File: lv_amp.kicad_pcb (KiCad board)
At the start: 2 copper layers, 127 x 76.2 mm, 85 parts, among them J1 Jack-DC, J2 AudioJack2, J3 AudioJack2, Q1 Q_NMOS_DGS, U1 MAX1771xSA, U2 TL072, U3 ECC83, U4 ECC83, U5 ECC83

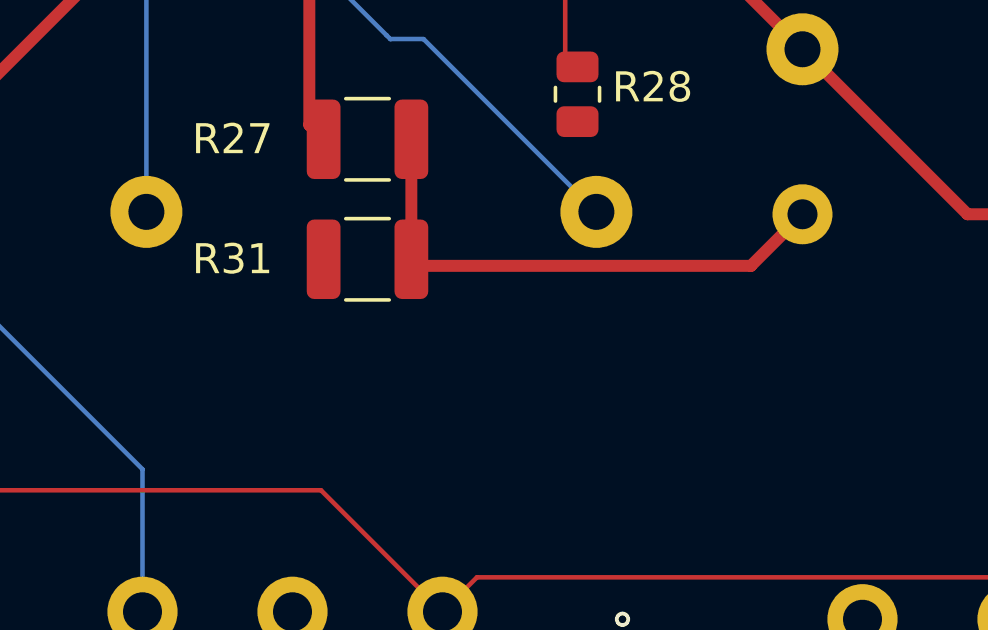
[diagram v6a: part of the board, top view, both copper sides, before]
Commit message: alpha0 errata: add 0ohm resistor for easier modding of stage 4
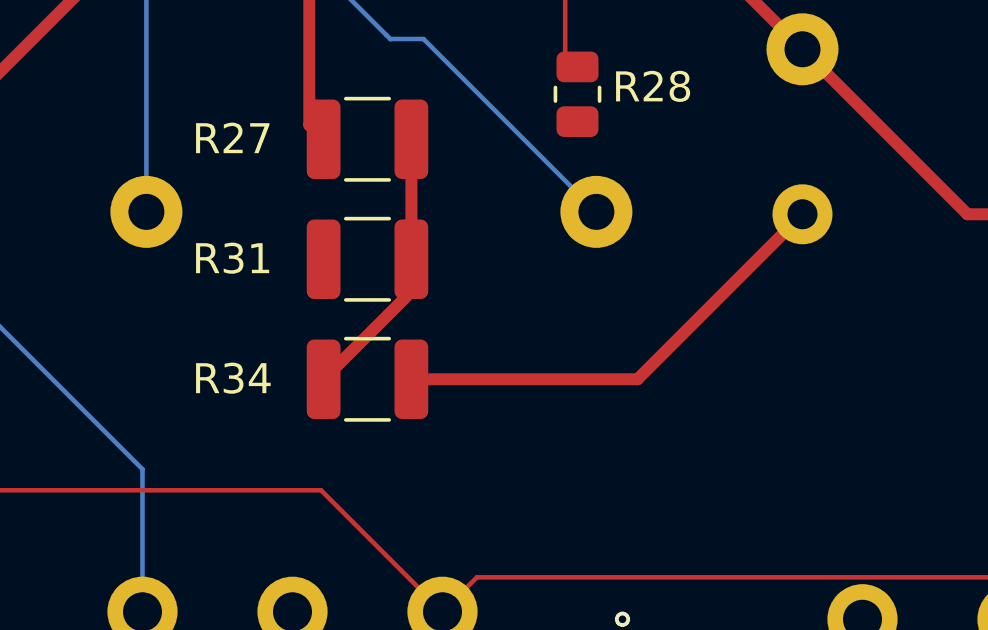
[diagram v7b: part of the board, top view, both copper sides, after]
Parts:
- added R34: 0, Resistor_SMD:R_1210_3225Metric, F.Cu at (81.5, 129.0)
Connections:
- C22 pad 2: /u3ap_couple -> /u3ap_couple_res
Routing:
- net /u3ap_couple_res: track 0.00 -> 15.3 mm
- net /u3ap_couple: track 17.8 -> 9.21 mm
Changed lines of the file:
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@@
   (net 54 "unconnected-(U5-Pad9)")
   (net 55 "/q1gr")
+  (net 56 "/u3ap_couple_res")
   (footprint "Capacitor_SMD:C_0603_1608Metric" (layer "F.Cu")
     (at 55 87 -90)
@@
   )
   (footprint "Resistor_SMD:R_1210_3225Metric" (layer "F.Cu")
+    (at 81.5 129)
+    (descr "Resistor SMD 1210 (3225 Metric), square (rectangular) end terminal, IPC_7351 nominal, (Body size source: IPC-SM-782 page 72, https://www.pcb-3d.com/wordpress/wp-content/uploads/ipc-sm-782a_amendment_1_and_2.pdf), generated with kicad-footprint-generator")
+    (tags "resistor")
+    (property "Sheetfile" "lv_amp.kicad_sch")
+    (property "Sheetname" "")
+    (attr smd)
+    (fp_text reference "R34" (at -4.5 0) (layer "F.SilkS")
+      (effects (font (size 1 1) (thickness 0.15)))
+    )
+    (fp_text value "0" (at 0 2.28) (layer "F.Fab")
+      (effects (font (size 1 1) (thickness 0.15)))
+    )
+    (fp_text user "${REFERENCE}" (at 0 0) (layer "F.Fab")
+      (effects (font (size 0.8 0.8) (thickness 0.12)))
+    )
+    (fp_line (start -0.723737 1.355) (end 0.723737 1.355) (layer "F.SilkS") (width 0.12))
+    (fp_line (start -0.723737 -1.355) (end 0.723737 -1.355) (layer "F.SilkS") (width 0.12))
+    (fp_line (start 2.28 1.58) (end -2.28 1.58) (layer "F.CrtYd") (width 0.05))
+    (fp_line (start 2.28 -1.58) (end 2.28 1.58) (layer "F.CrtYd") (width 0.05))
+    (fp_line (start -2.28 -1.58) (end 2.28 -1.58) (layer "F.CrtYd") (width 0.05))
+    (fp_line (start -2.28 1.58) (end -2.28 -1.58) (layer "F.CrtYd") (width 0.05))
+    (fp_line (start -1.6 1.245) (end -1.6 -1.245) (layer "F.Fab") (width 0.1))
+    (fp_line (start 1.6 -1.245) (end 1.6 1.245) (layer "F.Fab") (width 0.1))
+    (fp_line (start -1.6 -1.245) (end 1.6 -1.245) (layer "F.Fab") (width 0.1))
+    (fp_line (start 1.6 1.245) (end -1.6 1.245) (layer "F.Fab") (width 0.1))
+    (pad "1" smd roundrect locked (at -1.4625 0) (size 1.125 2.65) (layers "F.Cu" "F.Paste" "F.Mask") (roundrect_rratio 0.222222)
+      (net 23 "/u3ap_couple") (pintype "passive"))
+    (pad "2" smd roundrect locked (at 1.4625 0) (size 1.125 2.65) (layers "F.Cu" "F.Paste" "F.Mask") (roundrect_rratio 0.222222)
+      (net 56 "/u3ap_couple_res") (pintype "passive"))
+    (model "${KICAD6_3DMODEL_DIR}/Resistor_SMD.3dshapes/R_1210_3225Metric.wrl"
+      (offset (xyz 0 0 0))
+      (scale (xyz 1 1 1))
+      (rotate (xyz 0 0 0))
+    )
+  )
+  (footprint "Resistor_SMD:R_1210_3225Metric" (layer "F.Cu")
     (at 81.5 125)
     (descr "Resistor SMD 1210 (3225 Metric), square (rectangular) end terminal, IPC_7351 nominal, (Body size source: IPC-SM-782 page 72, https://www.pcb-3d.com/wordpress/wp-content/uploads/ipc-sm-782a_amendment_1_and_2.pdf), generated with kicad-footprint-generator")
@@
       (net 22 "/u3ap") (pintype "passive"))
     (pad "2" thru_hole circle locked (at 10 0 180) (size 2 2) (drill 1) (layers *.Cu *.Mask)
-      (net 23 "/u3ap_couple") (pintype "passive"))
+      (net 56 "/u3ap_couple_res") (pintype "passive"))
     (model "${KICAD6_3DMODEL_DIR}/Capacitor_THT.3dshapes/C_Rect_L13.0mm_W4.0mm_P10.00mm_FKS3_FKP3_MKS4.wrl"
       (offset (xyz 0 0 0))
@@
   (segment (start 92 108) (end 89.9625 108) (width 0.4) (layer "F.Cu") (net 22))
   (segment (start 101.5 123.5) (end 106 123.5) (width 0.4) (layer "F.Cu") (net 22))
+  (segment (start 82.9625 125) (end 82.9625 126.075) (width 0.4) (layer "F.Cu") (net 23))
   (segment (start 82.9625 121) (end 82.9625 125) (width 0.4) (layer "F.Cu") (net 23))
-  (segment (start 83.182011 125.219511) (end 82.9625 125) (width 0.4) (layer "F.Cu") (net 23))
-  (segment (start 96 123.5) (end 94.280489 125.219511) (width 0.4) (layer "F.Cu") (net 23))
-  (segment (start 94.280489 125.219511) (end 83.182011 125.219511) (width 0.4) (layer "F.Cu") (net 23))
+  (segment (start 82.9625 126.075) (end 80.0375 129) (width 0.4) (layer "F.Cu") (net 23))
   (segment (start 57.825 124.875) (end 60.5 124.875) (width 0.1524) (layer "F.Cu") (net 24))
   (segment (start 78.5375 109) (end 78.5375 109.4625) (width 0.4) (layer "F.Cu") (net 25))
@@
   (segment (start 126.75 90.425) (end 128.175 89) (width 1) (layer "F.Cu") (net 55))
   (segment (start 125.905 90.425) (end 126.75 90.425) (width 1) (layer "F.Cu") (net 55))
+  (segment (start 82.9625 129) (end 90.5 129) (width 0.4) (layer "F.Cu") (net 56))
+  (segment (start 90.5 129) (end 96 123.5) (width 0.4) (layer "F.Cu") (net 56))
   (zone (net 9) (net_name "GND") (layers F&B.Cu) (hatch edge 0.508)
     (connect_pads (clearance 0.508))

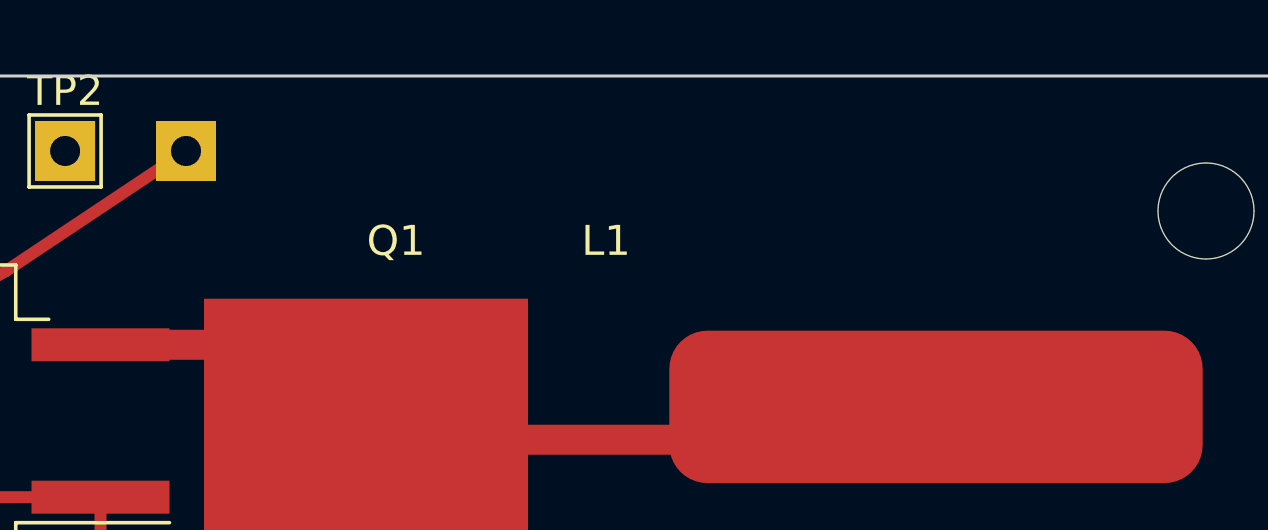
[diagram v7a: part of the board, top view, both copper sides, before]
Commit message: alpha0 errata: add slot for load resistor for testing
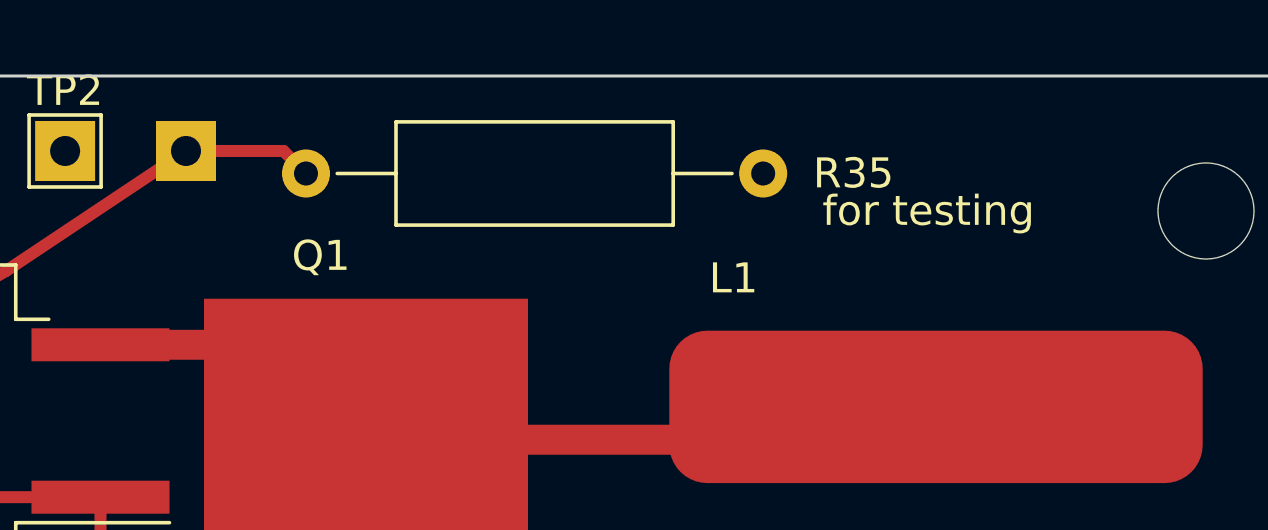
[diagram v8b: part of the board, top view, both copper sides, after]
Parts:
- added R35: N/C Load, Resistor_THT:R_Axial_DIN0309_L9.0mm_D3.2mm_P15.24mm_Horizontal, F.Cu at (130.0, 66.8)
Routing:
- net HT: track 197.1 -> 201.4 mm
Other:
- board text added: "for testing"
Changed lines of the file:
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@@
     (property "Sheetname" "")
     (attr smd)
-    (fp_text reference "L1" (at 19.5 -11 unlocked) (layer "F.SilkS")
+    (fp_text reference "L1" (at 18.25 -6.75 unlocked) (layer "F.SilkS")
       (effects (font (size 1 1) (thickness 0.15)))
     )
@@
       (net 7 "Net-(C12-Pad2)") (pintype "passive"))
     (model "${KICAD6_3DMODEL_DIR}/Resistor_SMD.3dshapes/R_1206_3216Metric.wrl"
+      (offset (xyz 0 0 0))
+      (scale (xyz 1 1 1))
+      (rotate (xyz 0 0 0))
+    )
+  )
+  (footprint "Resistor_THT:R_Axial_DIN0309_L9.0mm_D3.2mm_P15.24mm_Horizontal" (layer "F.Cu")
+    (at 130 66.75)
+    (descr "Resistor, Axial_DIN0309 series, Axial, Horizontal, pin pitch=15.24mm, 0.5W = 1/2W, length*diameter=9*3.2mm^2, http://cdn-reichelt.de/documents/datenblatt/B400/1_4W%23YAG.pdf")
+    (tags "Resistor Axial_DIN0309 series Axial Horizontal pin pitch 15.24mm 0.5W = 1/2W length 9mm diameter 3.2mm")
+    (property "Sheetfile" "lv_amp.kicad_sch")
+    (property "Sheetname" "")
+    (attr through_hole)
+    (fp_text reference "R35" (at 18.25 0) (layer "F.SilkS")
+      (effects (font (size 1 1) (thickness 0.15)))
+    )
+    (fp_text value "N/C Load" (at 7.62 2.72) (layer "F.Fab")
+      (effects (font (size 1 1) (thickness 0.15)))
+    )
+    (fp_text user "${REFERENCE}" (at 7.62 0) (layer "F.Fab")
+      (effects (font (size 1 1) (thickness 0.15)))
+    )
+    (fp_line (start 3 1.72) (end 12.24 1.72) (layer "F.SilkS") (width 0.12))
+    (fp_line (start 12.24 1.72) (end 12.24 -1.72) (layer "F.SilkS") (width 0.12))
+    (fp_line (start 3 -1.72) (end 3 1.72) (layer "F.SilkS") (width 0.12))
+    (fp_line (start 14.2 0) (end 12.24 0) (layer "F.SilkS") (width 0.12))
+    (fp_line (start 1.04 0) (end 3 0) (layer "F.SilkS") (width 0.12))
+    (fp_line (start 12.24 -1.72) (end 3 -1.72) (layer "F.SilkS") (width 0.12))
+    (fp_line (start 16.29 -1.85) (end -1.05 -1.85) (layer "F.CrtYd") (width 0.05))
+    (fp_line (start 16.29 1.85) (end 16.29 -1.85) (layer "F.CrtYd") (width 0.05))
+    (fp_line (start -1.05 -1.85) (end -1.05 1.85) (layer "F.CrtYd") (width 0.05))
+    (fp_line (start -1.05 1.85) (end 16.29 1.85) (layer "F.CrtYd") (width 0.05))
+    (fp_line (start 12.12 1.6) (end 12.12 -1.6) (layer "F.Fab") (width 0.1))
+    (fp_line (start 15.24 0) (end 12.12 0) (layer "F.Fab") (width 0.1))
+    (fp_line (start 0 0) (end 3.12 0) (layer "F.Fab") (width 0.1))
+    (fp_line (start 12.12 -1.6) (end 3.12 -1.6) (layer "F.Fab") (width 0.1))
+    (fp_line (start 3.12 1.6) (end 12.12 1.6) (layer "F.Fab") (width 0.1))
+    (fp_line (start 3.12 -1.6) (end 3.12 1.6) (layer "F.Fab") (width 0.1))
+    (pad "1" thru_hole circle locked (at 0 0) (size 1.6 1.6) (drill 0.8) (layers *.Cu *.Mask)
+      (net 21 "HT") (pintype "passive"))
+    (pad "2" thru_hole oval locked (at 15.24 0) (size 1.6 1.6) (drill 0.8) (layers *.Cu *.Mask)
+      (net 9 "GND") (pintype "passive"))
+    (model "${KICAD6_3DMODEL_DIR}/Resistor_THT.3dshapes/R_Axial_DIN0309_L9.0mm_D3.2mm_P15.24mm_Horizontal.wrl"
       (offset (xyz 0 0 0))
       (scale (xyz 1 1 1))
@@
     (property "Sheetname" "")
     (attr smd)
-    (fp_text reference "Q1" (at 10 1) (layer "F.SilkS")
+    (fp_text reference "Q1" (at 9.5 -1.5) (layer "F.SilkS")
       (effects (font (size 1 1) (thickness 0.15)))
     )
@@
   (gr_text "lv-amp alpha0" (at 140 80) (layer "B.SilkS")
     (effects (font (size 1 1) (thickness 0.15)) (justify mirror))
+  )
+  (gr_text "for testing" (at 150.75 68) (layer "F.SilkS")
+    (effects (font (size 1 1) (thickness 0.15)))
   )
   (segment (start 57 86.175) (end 59 86.175) (width 0.1524) (layer "F.Cu") (net 1))
@@
   (segment (start 86.5 108) (end 92 102.5) (width 0.4) (layer "F.Cu") (net 21))
   (segment (start 114 82.1) (end 114 75) (width 0.4) (layer "F.Cu") (net 21))
+  (segment (start 126 66) (end 129.25 66) (width 0.4) (layer "F.Cu") (net 21))
   (segment (start 110.85 85.25) (end 106.53 80.93) (width 0.4) (layer "F.Cu") (net 21))
   (segment (start 110.85 85.25) (end 114 82.1) (width 0.4) (layer "F.Cu") (net 21))
@@
   (segment (start 126 66) (end 120 70) (width 0.4) (layer "F.Cu") (net 21))
   (segment (start 114.79952 110.79952) (end 113 109) (width 0.4) (layer "F.Cu") (net 21))
+  (segment (start 129.25 66) (end 130 66.75) (width 0.4) (layer "F.Cu") (net 21))
   (segment (start 99.100489 81.349511) (end 74.164391 81.349511) (width 0.4) (layer "F.Cu") (net 21))
   (segment (start 123.15 77.54) (end 123.15 81.8875) (width 0.4) (layer "F.Cu") (net 21))
